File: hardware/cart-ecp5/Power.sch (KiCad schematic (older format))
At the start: 47 parts, among them U12 TPS2121, U13 TLV62568DBV, U5 TPS2111A, U6 TLV62568DBV, U7 TLV62568DBV, U8 TLV73325PDBV

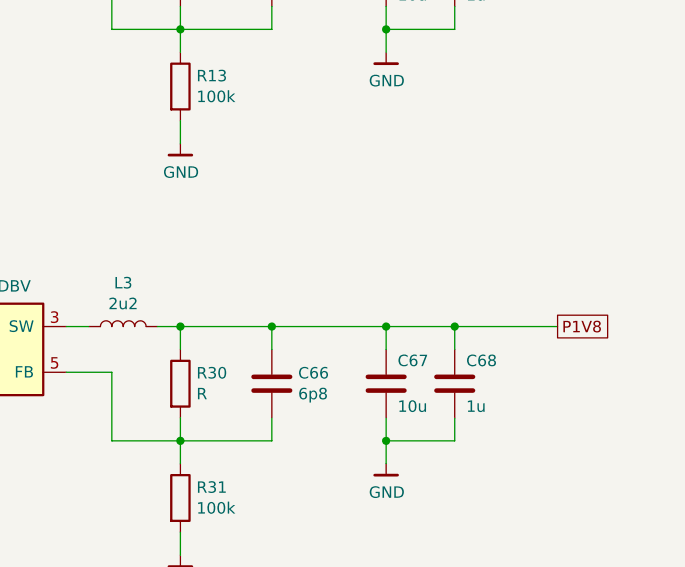
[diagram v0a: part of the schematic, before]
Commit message: Use 1V8 for HyperRAM interface
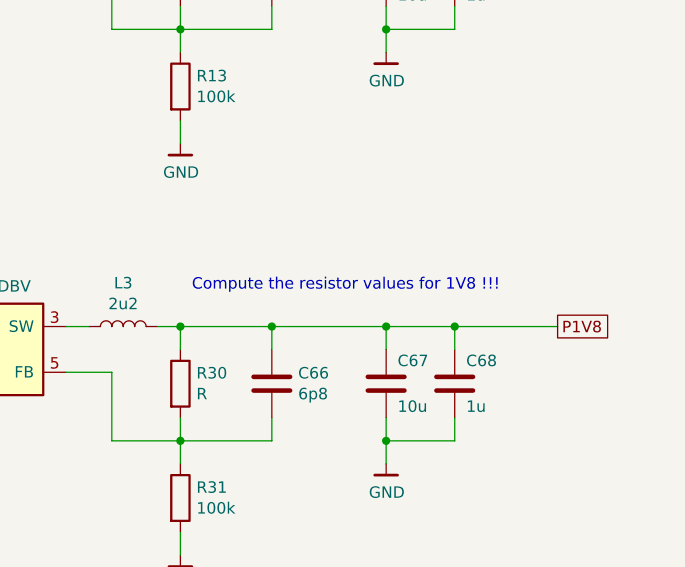
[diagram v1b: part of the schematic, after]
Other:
- note added: "Compute the resistor values for 1V8 !!!"
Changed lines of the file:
@@
 Text GLabel 6550 5000 0    50   UnSpc ~ 0
 P3V3
+Text Notes 8500 4850 0    50   ~ 0
+Compute the resistor values for 1V8 !!!
 $EndSCHEMATC

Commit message: Fanout MicroSD and N64 interfaces on the top layer
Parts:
- removed C63: 10u, Capacitor_SMD:C_0603_1608Metric, symbol Device:C
- removed C64: 10n, Capacitor_SMD:C_0402_1005Metric, symbol Device:C
- removed JP1, JP2, JP3: SolderJumper_2_Open, Jumper:SolderJumper-2_P1.3mm_Open_TrianglePad1.0x1.5mm, symbol Jumper:SolderJumper_2_Open
- removed R25, R27: 23k7, Resistor_SMD:R_0402_1005Metric, symbol Device:R
- removed R26, R28: 5k1, Resistor_SMD:R_0402_1005Metric, symbol Device:R
- removed R29: 47k, Resistor_SMD:R_0402_1005Metric, symbol Device:R
- removed U12: TPS2121, ng_package_qfn:Texas_VQFN-HR-12, symbol ng_pmic:TPS2121
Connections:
- net labels removed: MUX_3V3
- wire segments 193 -> 140
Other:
- note removed: "These values were derived from Butterstick!\nThey must be CHECKED !!!"
- moved on the sheet: C10, C11, C12, C13, C14, C15, C16, C17, C18, C19, C5, C6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

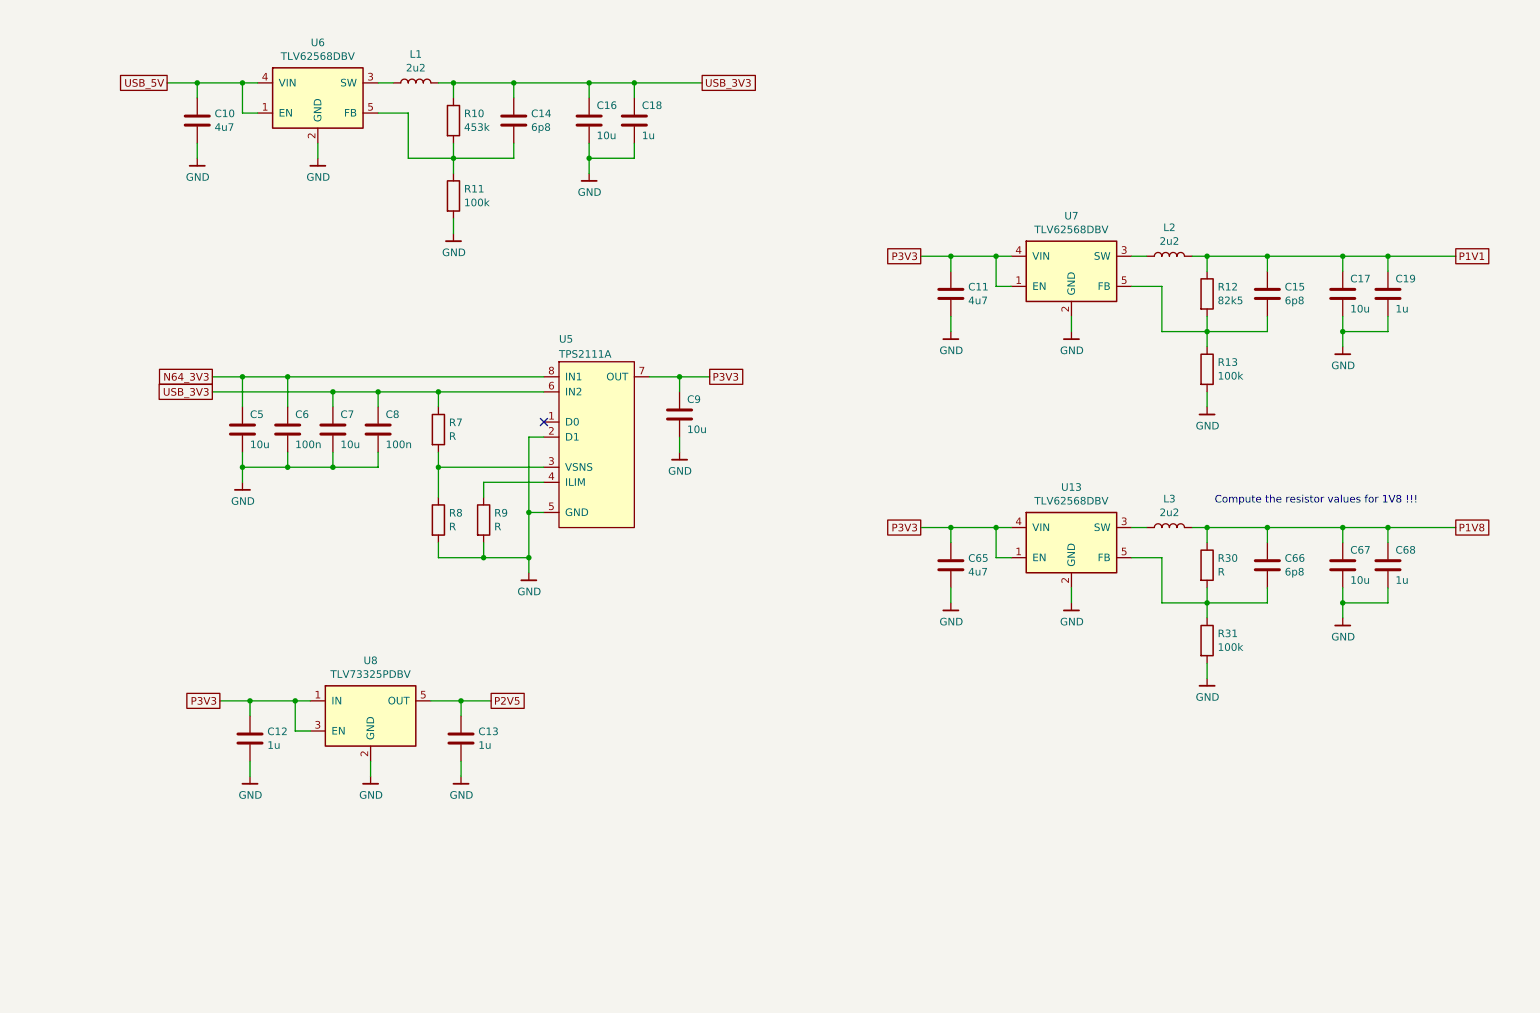
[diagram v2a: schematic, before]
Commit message: Route P1V8 switcher with traces and zones
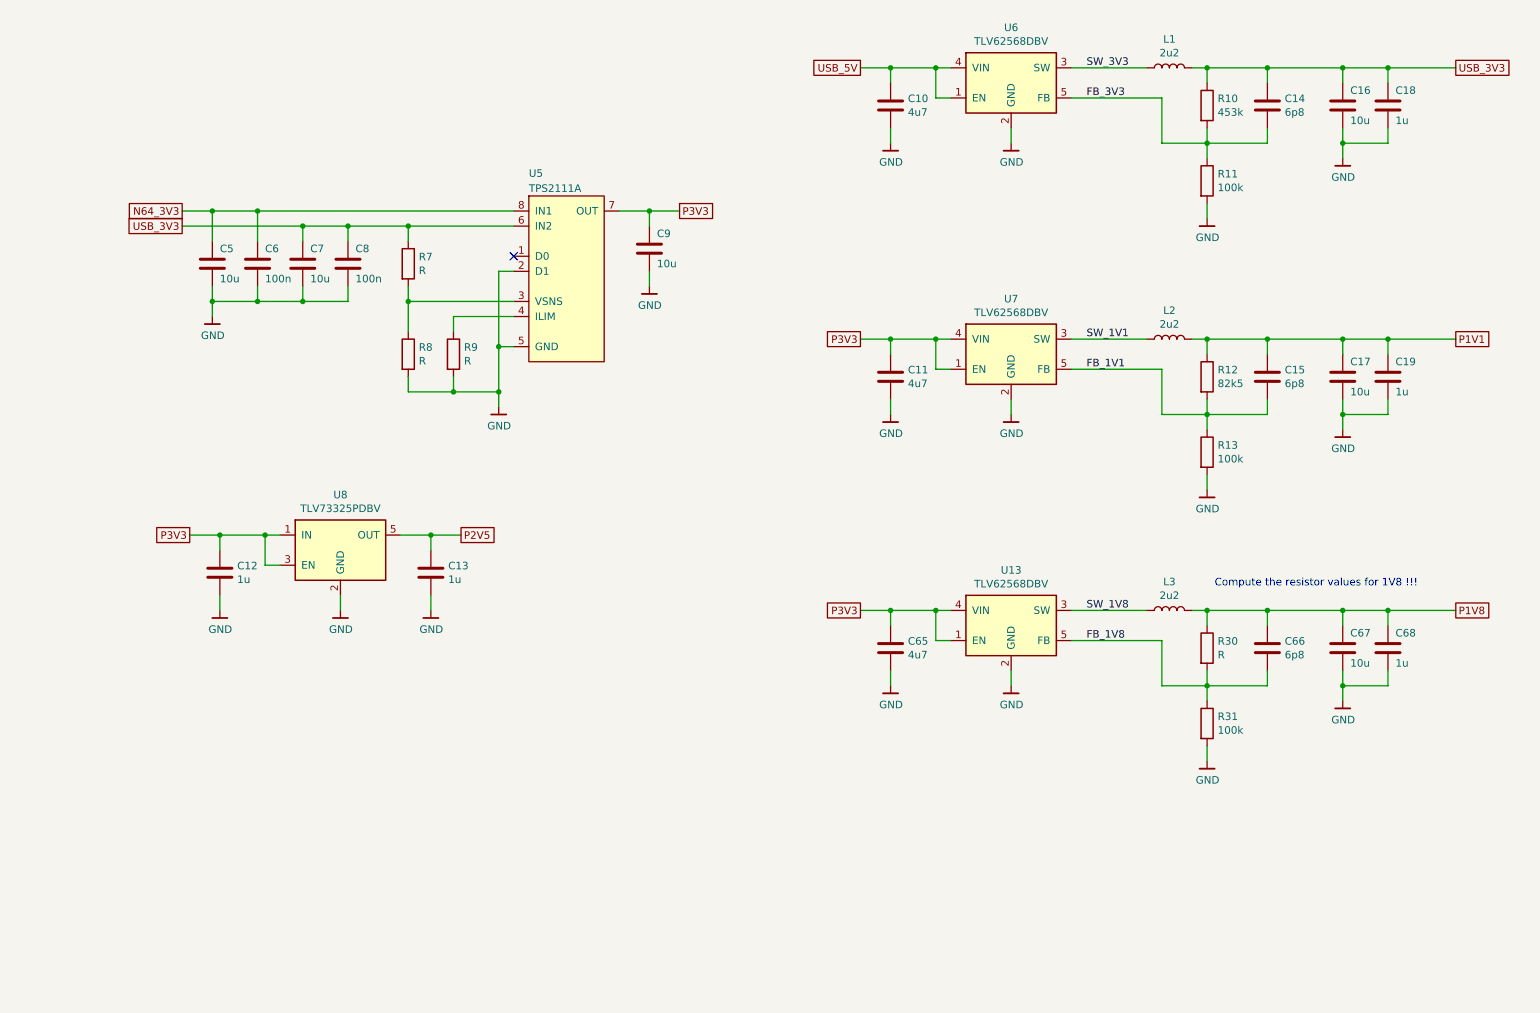
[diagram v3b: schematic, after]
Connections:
- net FB_1V1: now reaches C15.2, R12.2, R13.1, U7.5 (FB)
- net SW_1V1: now reaches L2.1, U7.3 (SW)
- net SW_3V3: now reaches L1.1, U6.3 (SW)
- net FB_3V3: now reaches C14.2, R10.2, R11.1, U6.5 (FB)
- net SW_1V8: now reaches L3.1, U13.3 (SW)
- net FB_1V8: now reaches C66.2, R30.2, R31.1, U13.5 (FB)
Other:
- moved on the sheet: C10, C11, C12, C13, C14, C15, C16, C17, C18, C19, C5, C6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

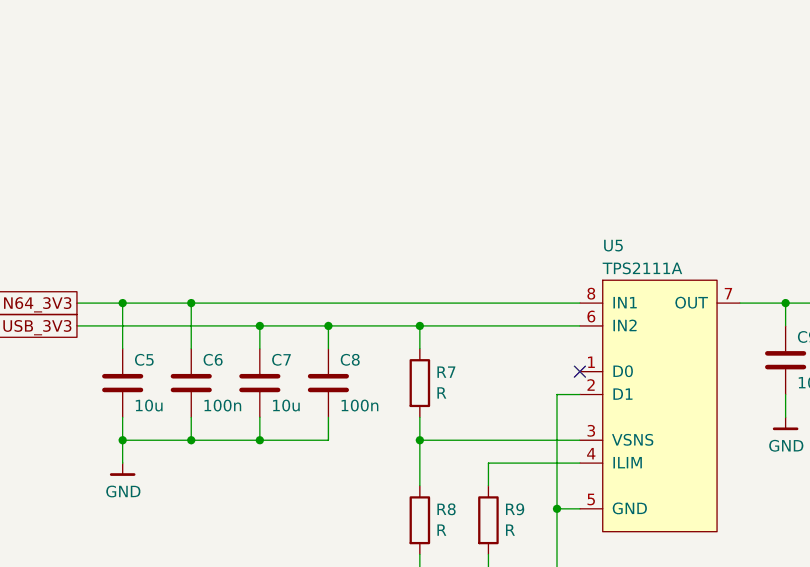
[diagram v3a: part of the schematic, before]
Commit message: Route power mux with traces
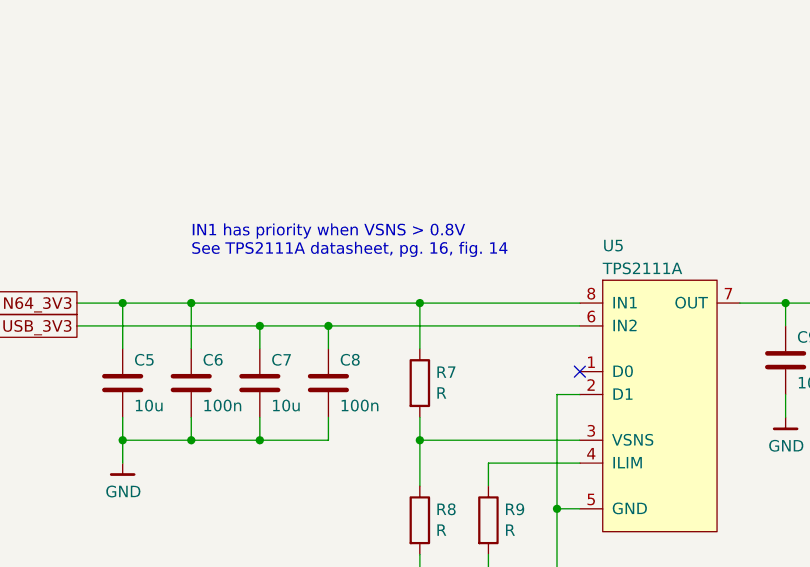
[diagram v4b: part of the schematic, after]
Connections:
- net N64_3V3: now also R7.1
- net USB_3V3: no longer R7.1
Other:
- note added: "IN1 has priority when VSNS > 0.8V\nSee TPS2111A datasheet, pg. 16, fig. 14"
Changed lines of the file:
@@
 	1900 2550 1900 2350
 Wire Wire Line
-	2200 2350 3900 2350
+	2200 2350 3200 2350
 Connection ~ 2200 2350
 Wire Wire Line
@@
 Wire Wire Line
 	2500 2550 2500 2450
-Wire Wire Line
-	2800 2450 3200 2450
 Connection ~ 2800 2450
 Wire Wire Line
@@
 Wire Wire Line
 	3900 2950 3200 2950
-Connection ~ 3200 2450
-Wire Wire Line
-	3200 2550 3200 2450
-Wire Wire Line
-	3900 2450 3200 2450
 $Comp
 L Device:R R7
@@
 Text Label 7700 1600 0    50   ~ 0
 FB_3V3
+Text Notes 2200 2150 0    50   ~ 0
+IN1 has priority when VSNS > 0.8V\nSee TPS2111A datasheet, pg. 16, fig. 14
+Wire Wire Line
+	2800 2450 3900 2450
+Wire Wire Line
+	3200 2550 3200 2350
+Connection ~ 3200 2350
+Wire Wire Line
+	3200 2350 3900 2350
 $EndSCHEMATC

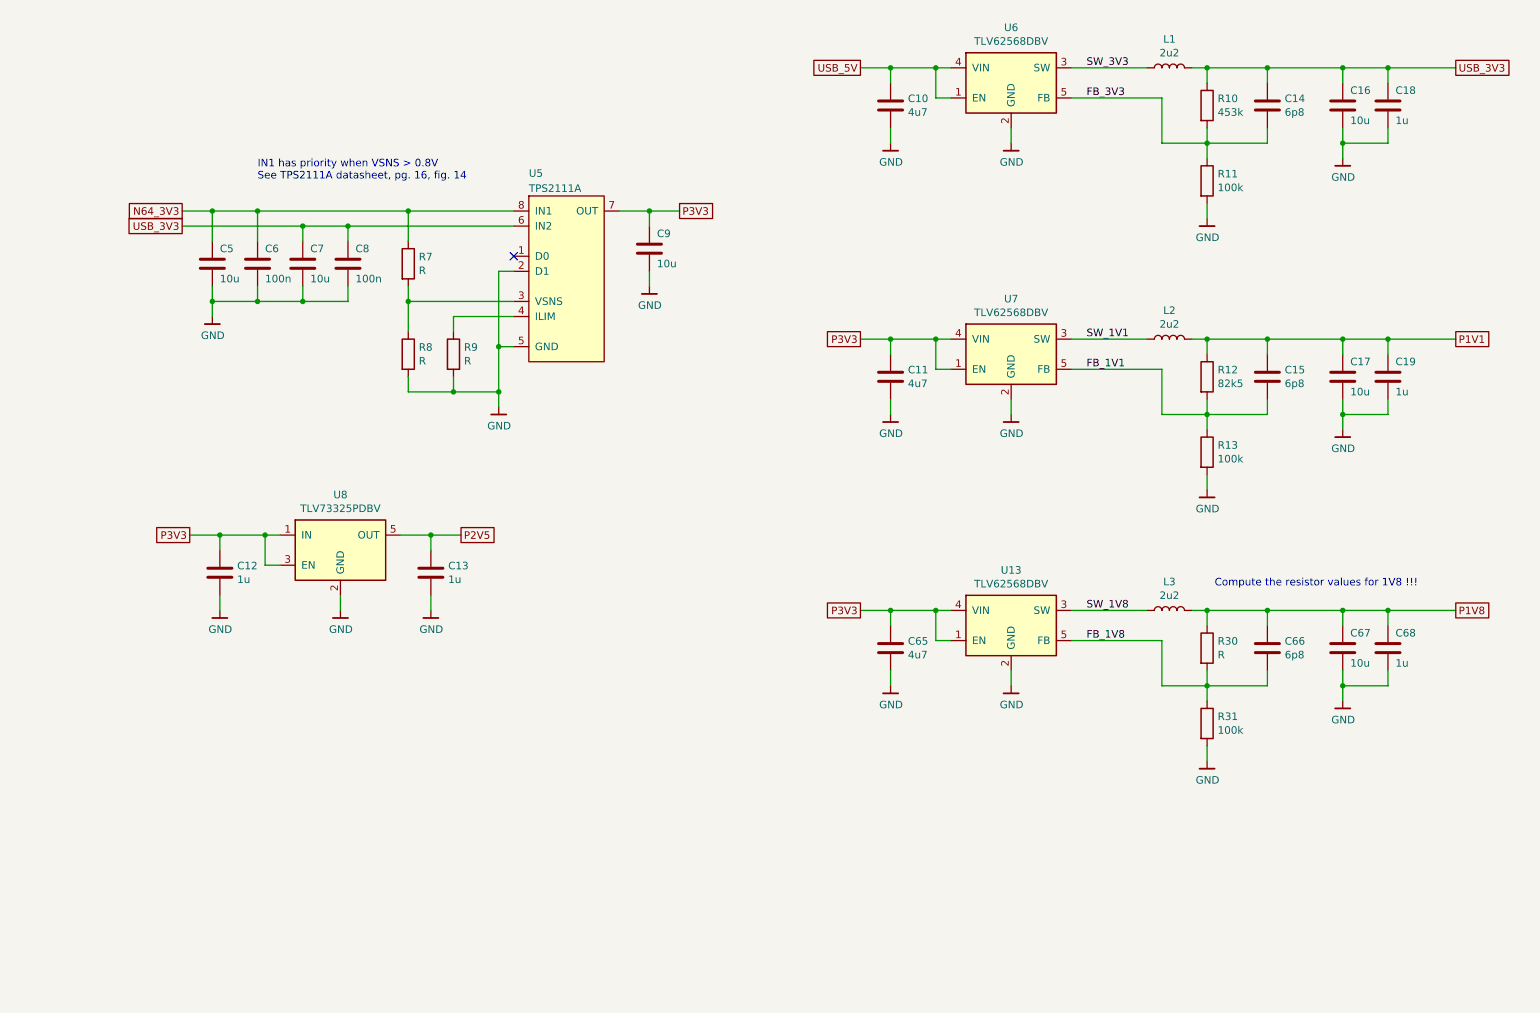
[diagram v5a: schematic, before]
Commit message: Add power rail test points to schematic
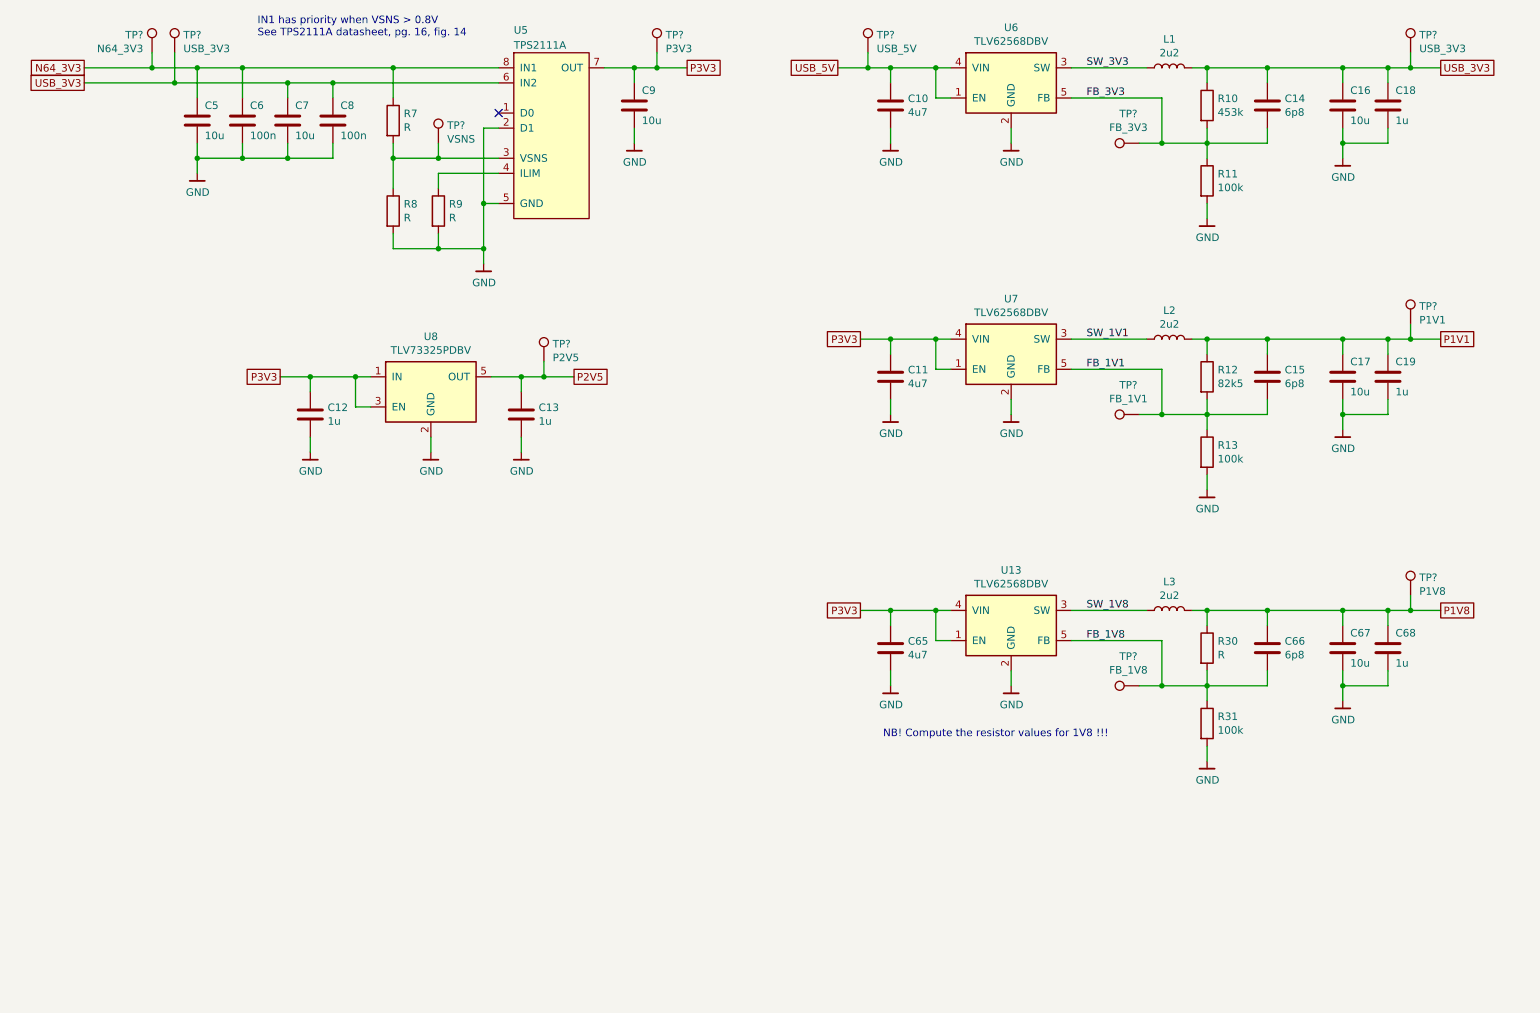
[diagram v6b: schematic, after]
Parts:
- added TP? (x2): USB_3V3, symbol Connector:TestPoint
- added TP?: P1V1, symbol Connector:TestPoint
- added TP?: P1V8, symbol Connector:TestPoint
- added TP?: P2V5, symbol Connector:TestPoint
- added TP?: USB_5V, symbol Connector:TestPoint
- added TP?: N64_3V3, symbol Connector:TestPoint
- added TP?: P3V3, symbol Connector:TestPoint
- added TP?: VSNS, symbol Connector:TestPoint
- added TP?: FB_3V3, symbol Connector:TestPoint
- added TP?: FB_1V1, symbol Connector:TestPoint
- added TP?: FB_1V8, symbol Connector:TestPoint
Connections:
- net FB_1V1: now also TP?.1
- net FB_1V8: now also TP?.1
- net FB_3V3: now also TP?.1
- net N64_3V3: now also TP?.1
- net P1V1: now also TP?.1
- net P1V8: now also TP?.1
- net P2V5: now also TP?.1
- net P3V3: now also TP?.1
- net USB_3V3: now also TP?.1, TP?.1
- net USB_5V: now also TP?.1
- net at R7.2, R8.1, U5.3 (VSNS): now also TP?.1
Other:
- note added: "NB! Compute the resistor values for 1V8 !!!"
- note removed: "Compute the resistor values for 1V8 !!!"
- moved on the sheet: C12, C13, C5, C6, C7, C8, C9, R7, R8, R9, U5, U8
